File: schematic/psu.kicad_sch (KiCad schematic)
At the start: 19 parts, among them J0 Conn_01x04

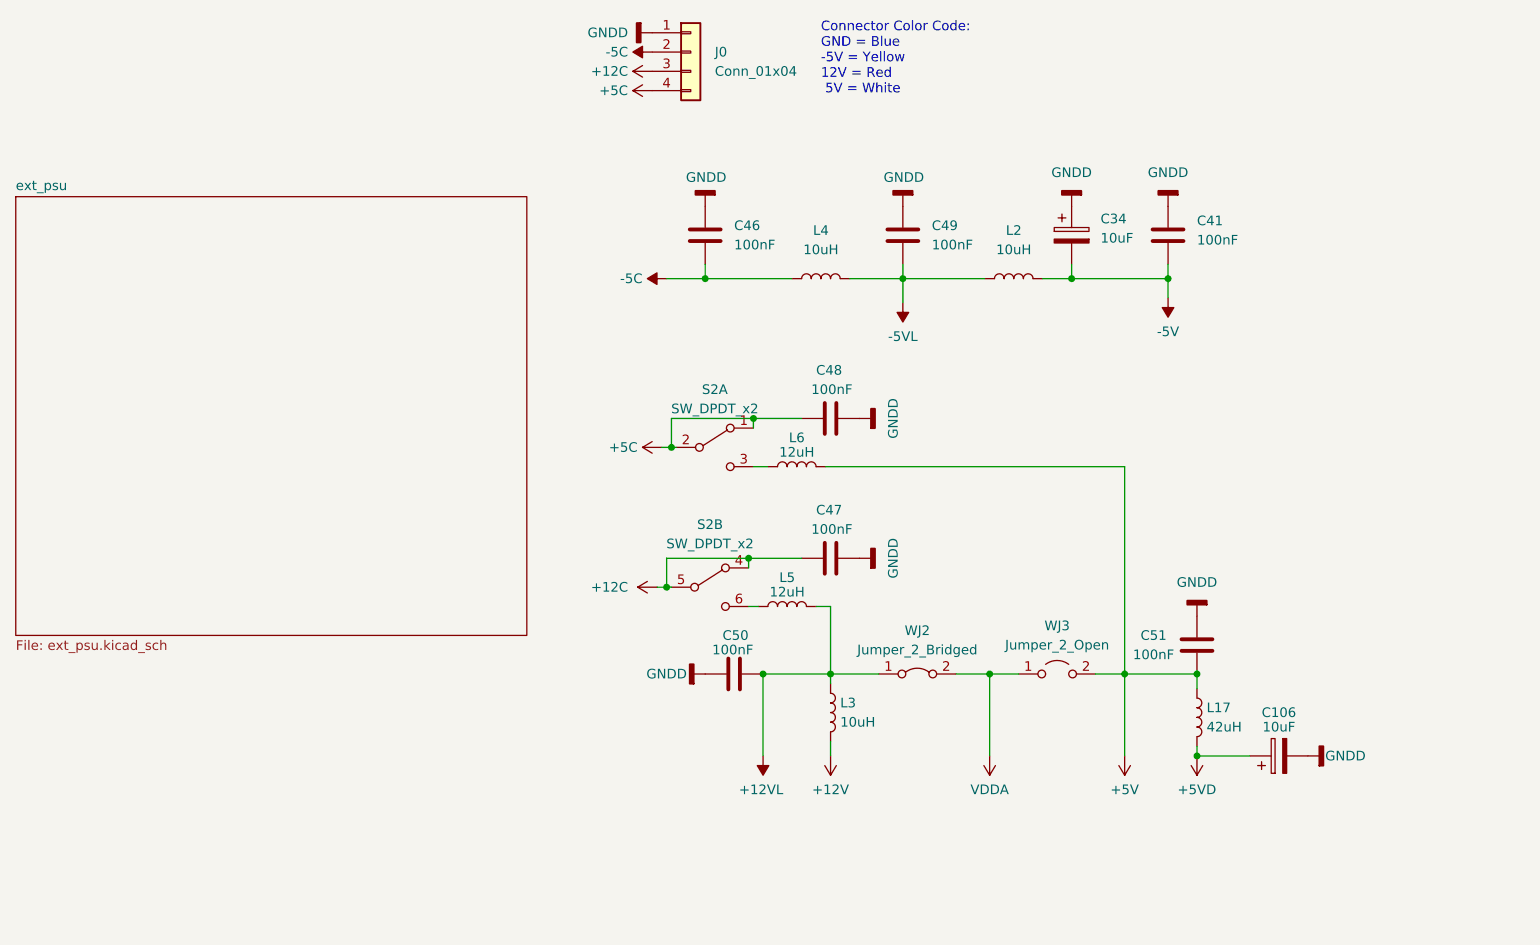
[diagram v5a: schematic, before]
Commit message: adjusted size of the sheets. added pcb version to the rev field. F.0... the 0 is for future fixes on my end. RF PCB is E.0.
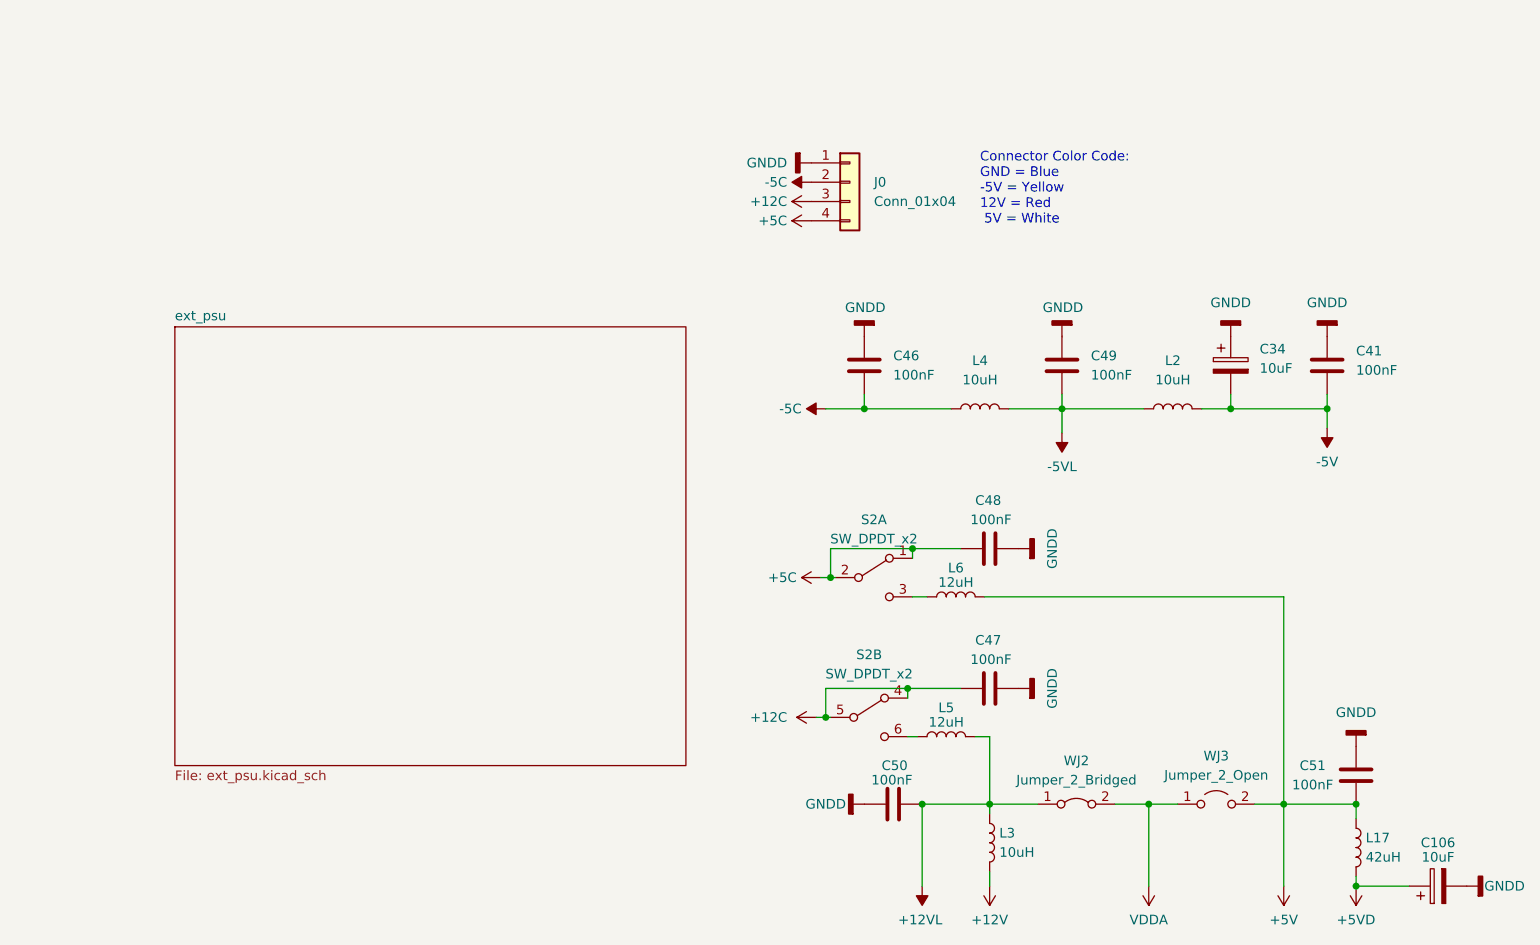
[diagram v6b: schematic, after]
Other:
- title: (none) -> Colecovision Schematic
- moved on the sheet: C106, C34, C41, C46, C47, C48, C49, C50, C51, J0, L17, L2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

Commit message: cleanup, and started associating components
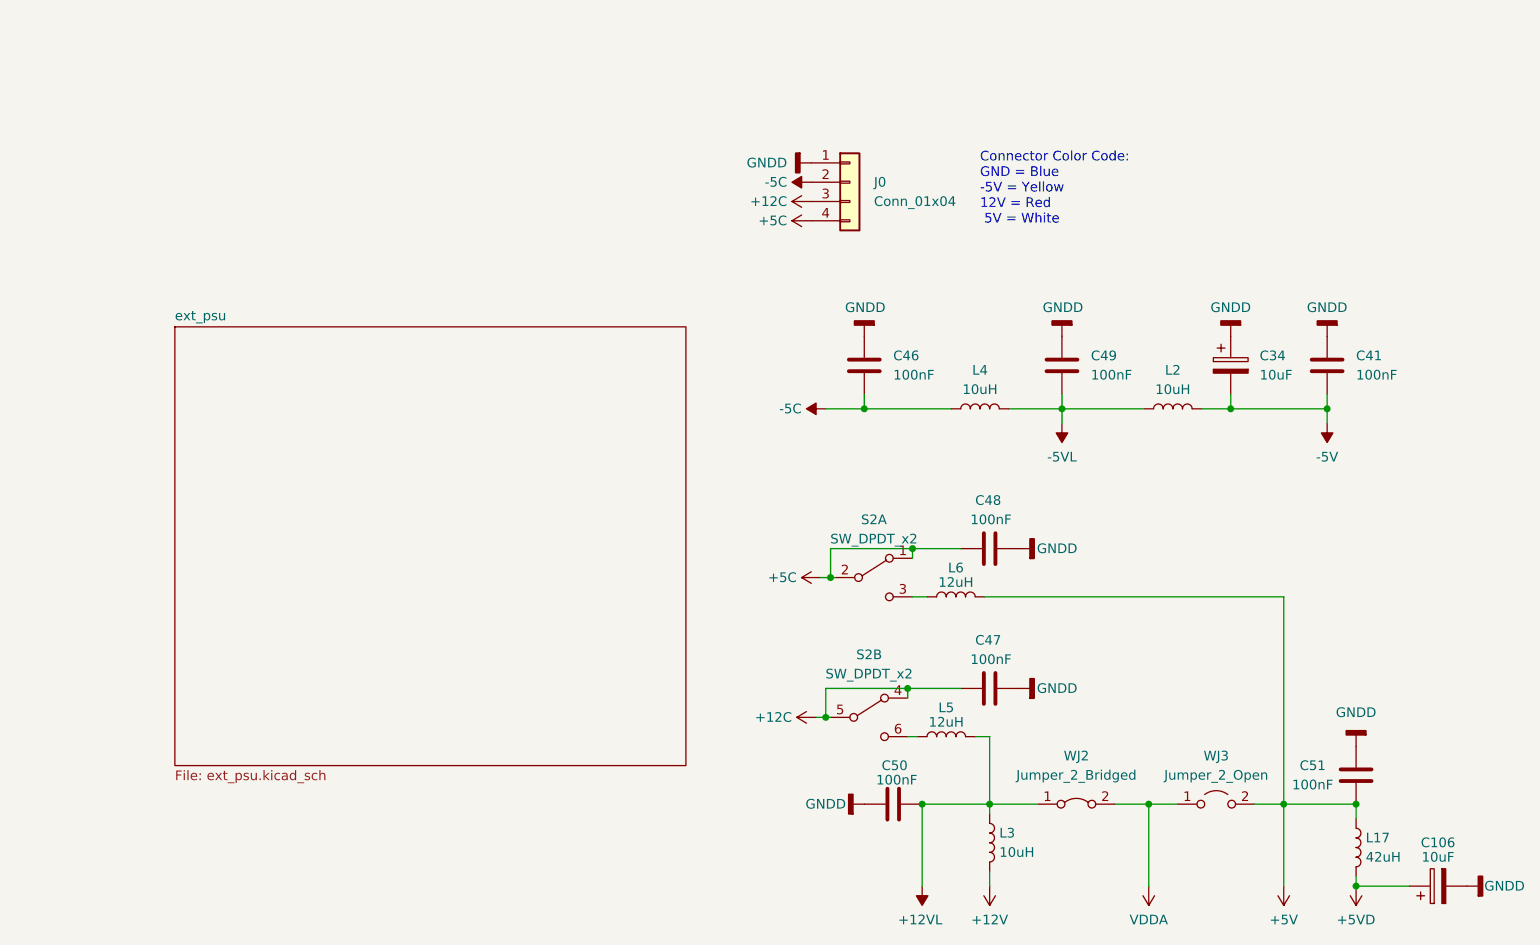
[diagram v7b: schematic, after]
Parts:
- C106, C34: footprint (none) -> Capacitor_THT:CP_Radial_D5.0mm_P2.00mm
- C41, C46, C47, C48, C49, C50, C51: footprint (none) -> Capacitor_THT:C_Disc_D10.0mm_W2.5mm_P5.00mm
- J0: footprint (none) -> Connector_Molex:Molex_KK-396_A-41791-0004_1x04_P3.96mm_Vertical
- L17, L2, L3, L4: footprint (none) -> Inductor_THT:L_Axial_L12.8mm_D5.8mm_P7.62mm_Vertical_Fastron_HBCC
- L5, L6: footprint (none) -> Inductor_THT:L_Axial_L12.0mm_D5.0mm_P15.24mm_Horizontal_Fastron_MISC
- S2: footprint (none) -> Button_Switch_THT:SW_E-Switch_EG1271_SPDT
- WJ2, WJ3: footprint (none) -> Resistor_THT:R_Bare_Metal_Element_L16.3mm_W4.8mm_P15.30mm

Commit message: added new libs for rest of the parts. some still need updating for correct parts, but for now they work. PCB import complete.
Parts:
- WJ2, WJ3: footprint Resistor_THT:R_Bare_Metal_Element_L16.3mm_W4.8mm_P15.30mm -> Resistor_THT:R_Axial_DIN0204_L3.6mm_D1.6mm_P7.62mm_Horizontal
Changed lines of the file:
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@@
     (property "Reference" "WJ2" (id 0) (at 167.005 120.65 0))
     (property "Value" "Jumper_2_Bridged" (id 1) (at 167.005 123.19 0))
-    (property "Footprint" "Resistor_THT:R_Bare_Metal_Element_L16.3mm_W4.8mm_P15.30mm" (id 2) (at 167.005 127 0)
+    (property "Footprint" "Resistor_THT:R_Axial_DIN0204_L3.6mm_D1.6mm_P7.62mm_Horizontal" (id 2) (at 167.005 127 0)
       (effects (font (size 1.27 1.27)) hide)
     )
@@
     (property "Reference" "WJ3" (id 0) (at 185.42 120.65 0))
     (property "Value" "Jumper_2_Open" (id 1) (at 185.42 123.19 0))
-    (property "Footprint" "Resistor_THT:R_Bare_Metal_Element_L16.3mm_W4.8mm_P15.30mm" (id 2) (at 185.42 127 0)
+    (property "Footprint" "Resistor_THT:R_Axial_DIN0204_L3.6mm_D1.6mm_P7.62mm_Horizontal" (id 2) (at 185.42 127 0)
       (effects (font (size 1.27 1.27)) hide)
     )
